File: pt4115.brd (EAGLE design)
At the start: 20.3 x 20.3 mm, 6 parts

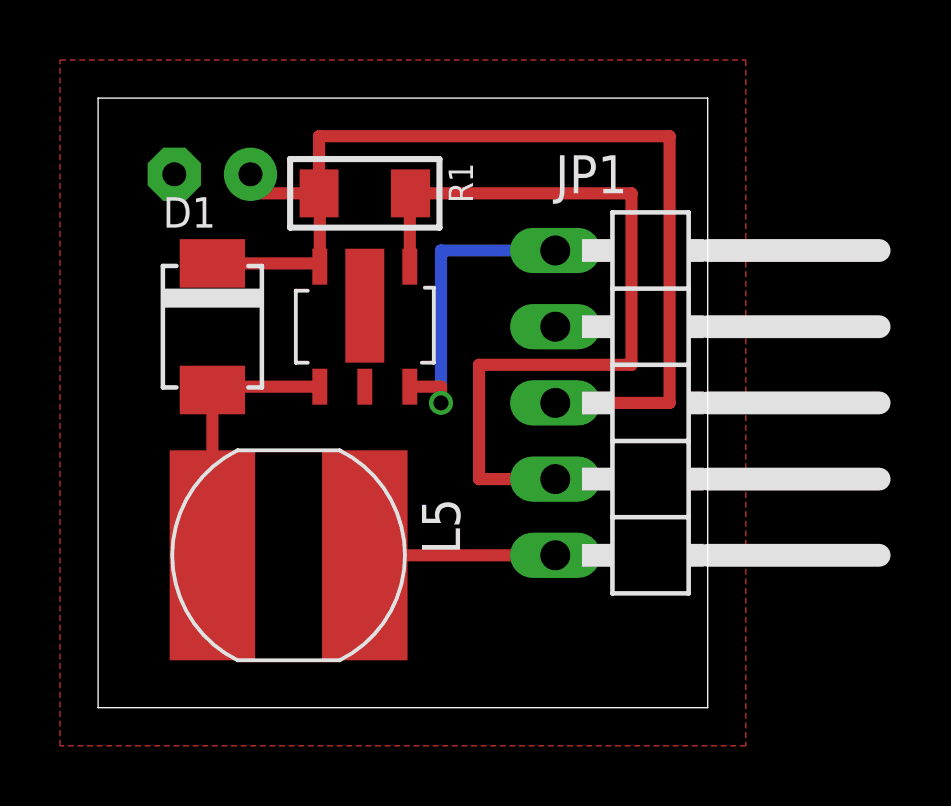
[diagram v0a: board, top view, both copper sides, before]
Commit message: fix PT4115 led driver
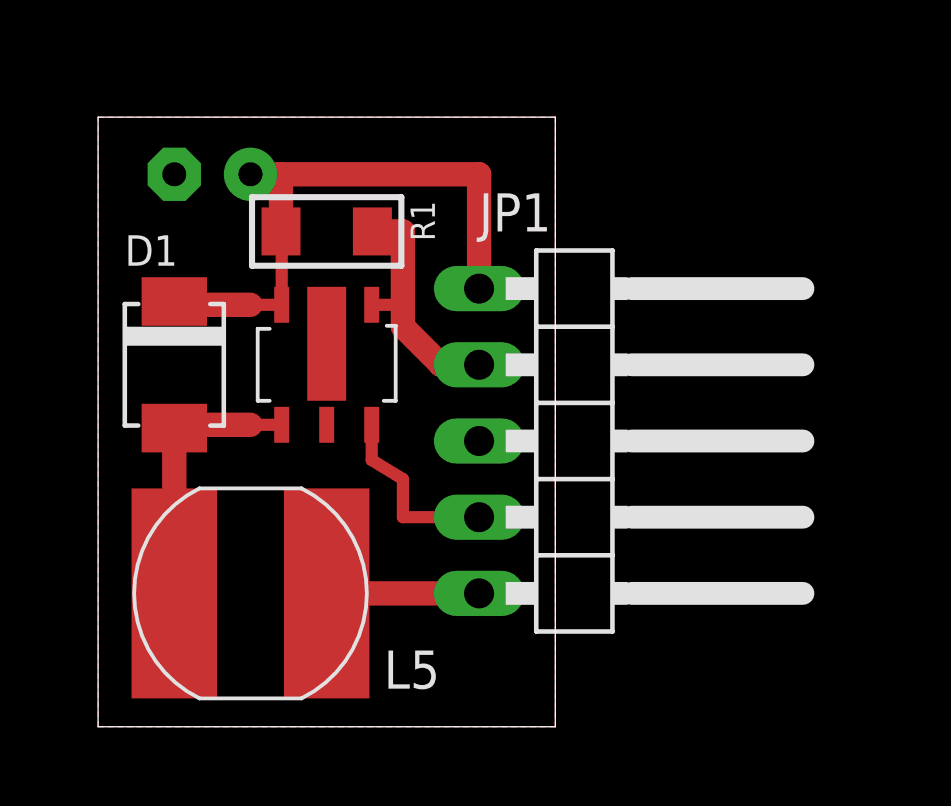
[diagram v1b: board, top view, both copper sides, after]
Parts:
- moved JP1 2.84 mm to (16.5, 8.89)
- moved D1 1.80 mm to (2.54, 11.4)
- moved L5 1.80 mm to (5.08, 3.81)
- moved R1 1.80 mm to (7.62, 15.9)
- moved U$13 1.80 mm to (7.62, 11.4)
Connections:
- net GND: now also JP1.3; no longer JP1.2
- net N$1: now also JP1.2; no longer JP1.4
- net N$3: now also JP1.4; no longer JP1.1
- net V+: now also JP1.1; no longer JP1.3
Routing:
- net N$1: track 27.0 -> 8.32 mm
- net V+: track 35.4 -> 19.5 mm
- net N$3: track 10.5 -> 6.20 mm, vias 1 -> 0
- net N$2: track 6.35 -> 5.08 mm
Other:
- board size 20.3 x 20.3 mm -> 15.2 x 20.3 mm
- board text added: "tuxotronic.org"
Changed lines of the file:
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@@
 <setting verticaltext="up"/>
 </settings>
-<grid distance="50" unitdist="mil" unit="mil" style="lines" multiple="1" display="yes" altdistance="0.025" altunitdist="inch" altunit="inch"/>
+<grid distance="1.27" unitdist="mm" unit="mm" style="lines" multiple="1" display="yes" altdistance="25" altunitdist="mil" altunit="mil"/>
 <layers>
 <layer number="1" name="Top" color="4" fill="1" visible="yes" active="yes"/>
@@
 <board>
 <plain>
-<wire x1="0" y1="0" x2="20.32" y2="0" width="0" layer="20"/>
-<wire x1="20.32" y1="0" x2="20.32" y2="20.32" width="0" layer="20"/>
-<wire x1="20.32" y1="20.32" x2="0" y2="20.32" width="0" layer="20"/>
-<wire x1="0" y1="20.32" x2="0" y2="0" width="0" layer="20"/>
-<text x="17.145" y="15.875" size="1.27" layer="22" ratio="16" rot="MR180">DM</text>
-<text x="17.145" y="13.335" size="1.27" layer="22" ratio="16" rot="MR180">V-</text>
-<text x="17.145" y="10.795" size="1.27" layer="22" ratio="16" rot="MR180">V+</text>
-<text x="17.145" y="8.255" size="1.27" layer="22" ratio="16" rot="MR180">L-</text>
-<text x="17.145" y="5.715" size="1.27" layer="22" ratio="16" rot="MR180">L+</text>
+<wire x1="0" y1="-0.635" x2="15.24" y2="-0.635" width="0" layer="20"/>
+<wire x1="15.24" y1="-0.635" x2="15.24" y2="19.685" width="0" layer="20"/>
+<wire x1="15.24" y1="19.685" x2="0" y2="19.685" width="0" layer="20"/>
+<wire x1="0" y1="19.685" x2="0" y2="-0.635" width="0" layer="20"/>
+<text x="8.255" y="6.985" size="1.27" layer="22" ratio="16" rot="MR180">DM</text>
+<text x="8.255" y="9.525" size="1.27" layer="22" ratio="16" rot="MR180">V-</text>
+<text x="8.255" y="14.605" size="1.27" layer="22" ratio="16" rot="MR180">V+</text>
+<text x="8.255" y="4.445" size="1.27" layer="22" ratio="16" rot="MR180">L-</text>
+<text x="8.255" y="12.065" size="1.27" layer="22" ratio="16" rot="MR180">L+</text>
+<text x="4.445" y="1.905" size="1.27" layer="22" ratio="16" rot="MR90">tuxotronic.org</text>
 </plain>
 <attributes>
@@
 </autorouter>
 <elements>
-<element name="U$13" library="1dah" package="SOT89-5" value="PT4115" x="8.89" y="12.7"/>
-<element name="R1" library="rc-master-smd" package="R1206" value="0.13" x="8.89" y="17.145" smashed="yes" rot="R180">
-<attribute name="NAME" x="11.684" y="18.161" size="0.8128" layer="25" ratio="18" rot="R270"/>
-<attribute name="VALUE" x="11.176" y="19.177" size="0.6096" layer="27" ratio="10" rot="R180"/>
+<element name="U$13" library="1dah" package="SOT89-5" value="PT4115" x="7.62" y="11.43"/>
+<element name="R1" library="rc-master-smd" package="R1206" value="0.13" x="7.62" y="15.875" smashed="yes" rot="R180">
+<attribute name="NAME" x="10.414" y="16.891" size="0.8128" layer="25" ratio="18" rot="R270"/>
+<attribute name="VALUE" x="9.906" y="17.907" size="0.6096" layer="27" ratio="10" rot="R180"/>
 </element>
-<element name="D1" library="diodes" package="SMB_1" value="STPS2L25U" x="3.81" y="12.7" smashed="yes" rot="R270">
-<attribute name="NAME" x="2.159" y="16.002" size="1.016" layer="25" ratio="18"/>
-<attribute name="VALUE" x="0.2286" y="14.986" size="1.27" layer="27" ratio="10" rot="R270"/>
+<element name="D1" library="diodes" package="SMB_1" value="STPS2L25U" x="2.54" y="11.43" smashed="yes" rot="R270">
+<attribute name="NAME" x="0.889" y="14.732" size="1.016" layer="25" ratio="18"/>
+<attribute name="VALUE" x="-1.0414" y="13.716" size="1.27" layer="27" ratio="10" rot="R270"/>
 </element>
-<element name="L5" library="rc-master-smd" package="CD75" value="68uH" x="6.35" y="5.08" smashed="yes" rot="R270">
-<attribute name="NAME" x="10.795" y="6.985" size="1.27" layer="25" ratio="16" rot="R270"/>
-<attribute name="VALUE" x="2.54" y="0" size="1.27" layer="27" ratio="16"/>
+<element name="L5" library="rc-master-smd" package="CD75" value="68uH" x="5.08" y="3.81" smashed="yes" rot="R270">
+<attribute name="NAME" x="9.525" y="0.635" size="1.27" layer="25" ratio="16"/>
+<attribute name="VALUE" x="1.27" y="-1.27" size="1.27" layer="27" ratio="16"/>
 </element>
 <element name="C1" library="rc-master" package="CE-025X060" value="100uF/35V" x="3.81" y="17.78" smashed="yes" rot="MR0">
-<attribute name="NAME" x="6.985" y="13.97" size="1.016" layer="26" ratio="18" rot="MR90"/>
+<attribute name="NAME" x="7.62" y="18.415" size="1.016" layer="26" ratio="18" rot="MR180"/>
 <attribute name="VALUE" x="0" y="14.605" size="0.8128" layer="28" ratio="10" rot="MR0"/>
 </element>
-<element name="JP1" library="pinhead-fixdrills" package="1X05/90" value="" x="19.05" y="10.16" rot="R270"/>
+<element name="JP1" library="pinhead-fixdrills" package="1X05/90" value="" x="16.51" y="8.89" rot="R270"/>
 </elements>
 <signals>
@@
 <contactref element="D1" pad="A"/>
 <contactref element="L5" pad="2"/>
-<wire x1="7.39" y1="10.7" x2="3.81" y2="10.7" width="0.4064" layer="1"/>
-<wire x1="3.81" y1="10.7" x2="3.81" y2="10.59" width="0.4064" layer="1"/>
-<wire x1="3.81" y1="5.08" x2="3.81" y2="10.59" width="0.4064" layer="1"/>
+<wire x1="6.12" y1="9.43" x2="5.08" y2="9.43" width="0.4064" layer="1"/>
+<wire x1="2.54" y1="3.81" x2="2.54" y2="9.32" width="0.8128" layer="1"/>
+<wire x1="5.08" y1="9.43" x2="2.54" y2="9.43" width="0.8128" layer="1"/>
+<wire x1="2.54" y1="9.43" x2="2.54" y2="9.32" width="0.8128" layer="1"/>
 </signal>
 <signal name="GND">
@@
 <contactref element="C1" pad="-"/>
 <polygon width="0.3048" layer="1" isolate="0.3048">
-<vertex x="-1.27" y="21.59"/>
-<vertex x="21.59" y="21.59"/>
-<vertex x="21.59" y="-1.27"/>
-<vertex x="-1.27" y="-1.27"/>
+<vertex x="0" y="19.685"/>
+<vertex x="15.24" y="19.685"/>
+<vertex x="15.24" y="-0.635"/>
+<vertex x="0" y="-0.635"/>
 </polygon>
-<contactref element="JP1" pad="2"/>
+<contactref element="JP1" pad="3"/>
 </signal>
 <signal name="N$1">
 <contactref element="U$13" pad="4"/>
 <contactref element="R1" pad="1"/>
-<contactref element="JP1" pad="4"/>
-<wire x1="15.24" y1="7.62" x2="12.7" y2="7.62" width="0.4064" layer="1"/>
-<wire x1="12.7" y1="7.62" x2="12.7" y2="11.43" width="0.4064" layer="1"/>
-<wire x1="12.7" y1="11.43" x2="17.78" y2="11.43" width="0.4064" layer="1"/>
-<wire x1="17.78" y1="11.43" x2="17.78" y2="17.145" width="0.4064" layer="1"/>
-<wire x1="10.414" y1="17.145" x2="17.78" y2="17.145" width="0.4064" layer="1"/>
-<wire x1="10.414" y1="17.145" x2="10.39" y2="17.145" width="0.4064" layer="1"/>
-<wire x1="10.39" y1="17.145" x2="10.39" y2="14.7" width="0.4064" layer="1"/>
-</signal>
-<signal name="N$3">
-<contactref element="U$13" pad="3"/>
-<contactref element="JP1" pad="1"/>
-<wire x1="10.39" y1="10.7" x2="11.43" y2="10.7" width="0.4064" layer="1"/>
-<wire x1="11.43" y1="10.7" x2="11.43" y2="10.16" width="0.4064" layer="1"/>
-<via x="11.43" y="10.16" extent="1-16" drill="0.5"/>
-<wire x1="11.43" y1="10.16" x2="11.43" y2="15.24" width="0.4064" layer="16"/>
-<wire x1="11.43" y1="15.24" x2="15.24" y2="15.24" width="0.4064" layer="16"/>
+<wire x1="9.144" y1="15.875" x2="9.12" y2="15.875" width="0.4064" layer="1"/>
+<contactref element="JP1" pad="2"/>
+<wire x1="12.7" y1="11.43" x2="11.43" y2="11.43" width="0.8128" layer="1"/>
+<wire x1="11.43" y1="11.43" x2="10.16" y2="12.7" width="0.8128" layer="1"/>
+<wire x1="10.16" y1="12.7" x2="10.16" y2="13.43" width="0.8128" layer="1"/>
+<wire x1="10.16" y1="13.43" x2="10.16" y2="15.875" width="0.8128" layer="1"/>
+<wire x1="9.144" y1="15.875" x2="10.16" y2="15.875" width="0.8128" layer="1"/>
+<wire x1="9.12" y1="13.43" x2="10.16" y2="13.43" width="0.4064" layer="1"/>
 </signal>
 <signal name="N$2">
 <contactref element="JP1" pad="5"/>
 <contactref element="L5" pad="1"/>
-<wire x1="8.89" y1="5.08" x2="15.24" y2="5.08" width="0.4064" layer="1"/>
+<wire x1="7.62" y1="3.81" x2="12.7" y2="3.81" width="0.8128" layer="1"/>
 </signal>
 <signal name="V+">
@@
 <contactref element="R1" pad="2"/>
 <contactref element="C1" pad="+"/>
-<wire x1="3.81" y1="14.81" x2="7.39" y2="14.81" width="0.4064" layer="1"/>
-<wire x1="7.39" y1="14.81" x2="7.39" y2="14.7" width="0.4064" layer="1"/>
-<wire x1="7.366" y1="17.145" x2="7.39" y2="17.145" width="0.4064" layer="1"/>
-<wire x1="7.39" y1="17.145" x2="7.39" y2="14.7" width="0.4064" layer="1"/>
-<contactref element="JP1" pad="3"/>
-<wire x1="7.366" y1="19.05" x2="7.366" y2="17.145" width="0.4064" layer="1"/>
-<wire x1="7.366" y1="19.05" x2="19.05" y2="19.05" width="0.4064" layer="1"/>
-<wire x1="19.05" y1="19.05" x2="19.05" y2="10.16" width="0.4064" layer="1"/>
-<wire x1="19.05" y1="10.16" x2="15.24" y2="10.16" width="0.4064" layer="1"/>
-<wire x1="7.366" y1="17.145" x2="5.08" y2="17.145" width="0.4064" layer="1"/>
-<wire x1="5.08" y1="17.145" x2="5.08" y2="17.78" width="0.4064" layer="1"/>
+<wire x1="6.096" y1="15.875" x2="6.12" y2="15.875" width="0.4064" layer="1"/>
+<wire x1="6.12" y1="15.875" x2="6.12" y2="13.43" width="0.4064" layer="1"/>
+<contactref element="JP1" pad="1"/>
+<wire x1="12.7" y1="13.97" x2="12.7" y2="17.78" width="0.8128" layer="1"/>
+<wire x1="12.7" y1="17.78" x2="6.096" y2="17.78" width="0.8128" layer="1"/>
+<wire x1="6.096" y1="17.78" x2="6.096" y2="15.875" width="0.8128" layer="1"/>
+<wire x1="5.08" y1="17.78" x2="6.096" y2="17.78" width="0.8128" layer="1"/>
+<wire x1="6.12" y1="13.43" x2="5.08" y2="13.43" width="0.4064" layer="1"/>
+<wire x1="5.08" y1="13.43" x2="2.54" y2="13.43" width="0.8128" layer="1"/>
+<wire x1="2.54" y1="13.43" x2="2.54" y2="13.54" width="0.8128" layer="1"/>
+</signal>
+<signal name="N$3">
+<contactref element="U$13" pad="3"/>
+<contactref element="JP1" pad="4"/>
+<wire x1="12.7" y1="6.35" x2="10.16" y2="6.35" width="0.4064" layer="1"/>
+<wire x1="10.16" y1="6.35" x2="10.16" y2="7.62" width="0.4064" layer="1"/>
+<wire x1="10.16" y1="7.62" x2="9.12" y2="8.255" width="0.4064" layer="1"/>
+<wire x1="9.12" y1="8.255" x2="9.12" y2="9.43" width="0.4064" layer="1"/>
 </signal>
 </signals>

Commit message: pt4115 fix to cd43 inductor
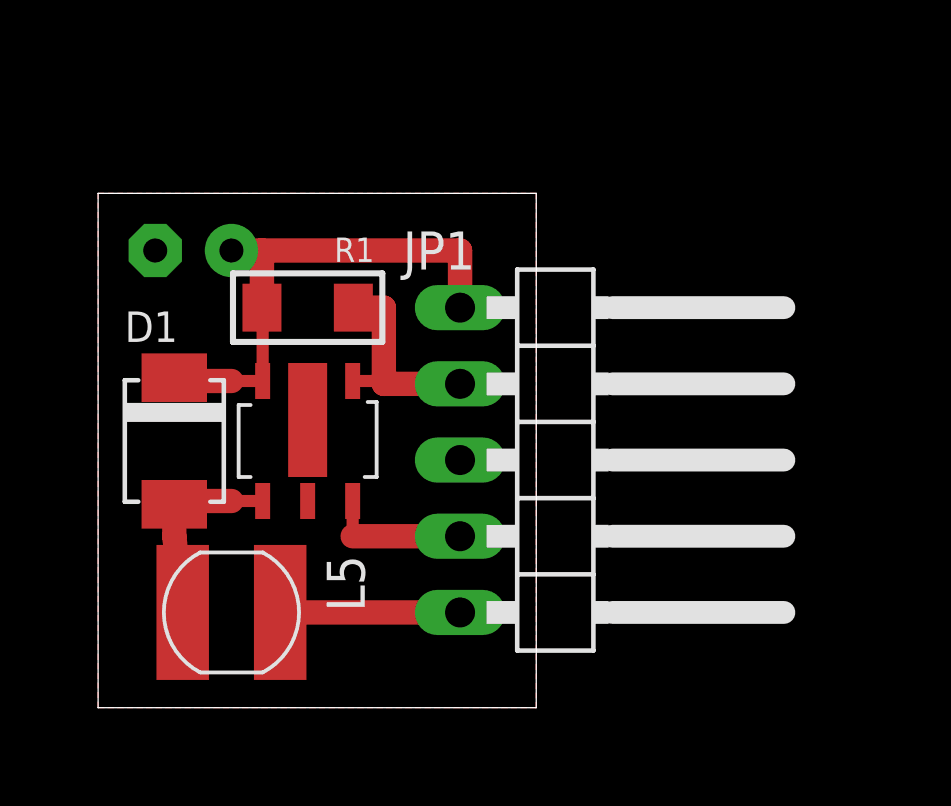
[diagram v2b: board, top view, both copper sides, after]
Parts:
- L5: device rc-master-smd:CD75 -> rc-master-smd:CD43
- moved C1 2.62 mm to (3.17, 15.2)
- moved R1 2.62 mm to (6.99, 13.3)
- moved U$13 2.62 mm to (6.99, 8.89)
- moved D1 2.54 mm to (2.54, 8.89)
- moved JP1 0.90 mm to (15.9, 8.26)
- moved L5 0.90 mm to (4.45, 3.17)
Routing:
- net N$3: track 6.20 -> 4.75 mm
- net V+: track 19.5 -> 18.1 mm
- net SW4: track 9.20 -> 7.84 mm
- net N$1: track 8.32 -> 7.16 mm
- net N$2: track 5.08 -> 5.99 mm
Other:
- board size 15.2 x 20.3 mm -> 14.6 x 17.1 mm

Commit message: pt4115 fixes
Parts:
- removed U$13: PT4115, 1dah:SOT89-5
- added C2: 0.1, rc-master-smd:C0805
- added DA1: PT4115, pt4115:SOT89-5
- L5: device rc-master-smd:CD43 -> rc-master-smd:CD54
- moved C1 0.90 mm to (2.54, 15.9)
- moved JP1 0.90 mm to (15.2, 8.89)
- moved D1 0.63 mm to (2.54, 9.53)
- moved L5 0.63 mm to (5.08, 3.17)
- moved R1 0.63 mm to (6.99, 14.0)
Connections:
- net GND: now also C2.2, DA1.2, DA1.PAD; no longer U$13.2, U$13.PAD
- net N$1: now also DA1.4; no longer U$13.4
- net N$3: now also DA1.3; no longer U$13.3
- net SW4: now also DA1.1; no longer U$13.1
- net V+: now also C2.1, DA1.5; no longer U$13.5
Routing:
- net GND: track 0.00 -> 3.65 mm, vias 0 -> 4
- net N$2: track 5.99 -> 4.73 mm
- net N$3: track 4.75 -> 3.88 mm
- net V+: track 18.1 -> 18.9 mm
- net N$1: track 7.16 -> 6.53 mm
- added copper zone on layer 16, net GND
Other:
- board size 14.6 x 17.1 mm -> 14 x 17.1 mm
